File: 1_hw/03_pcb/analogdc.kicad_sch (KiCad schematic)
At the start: 12 parts, among them U25 LM6171, U26 TMUX6104

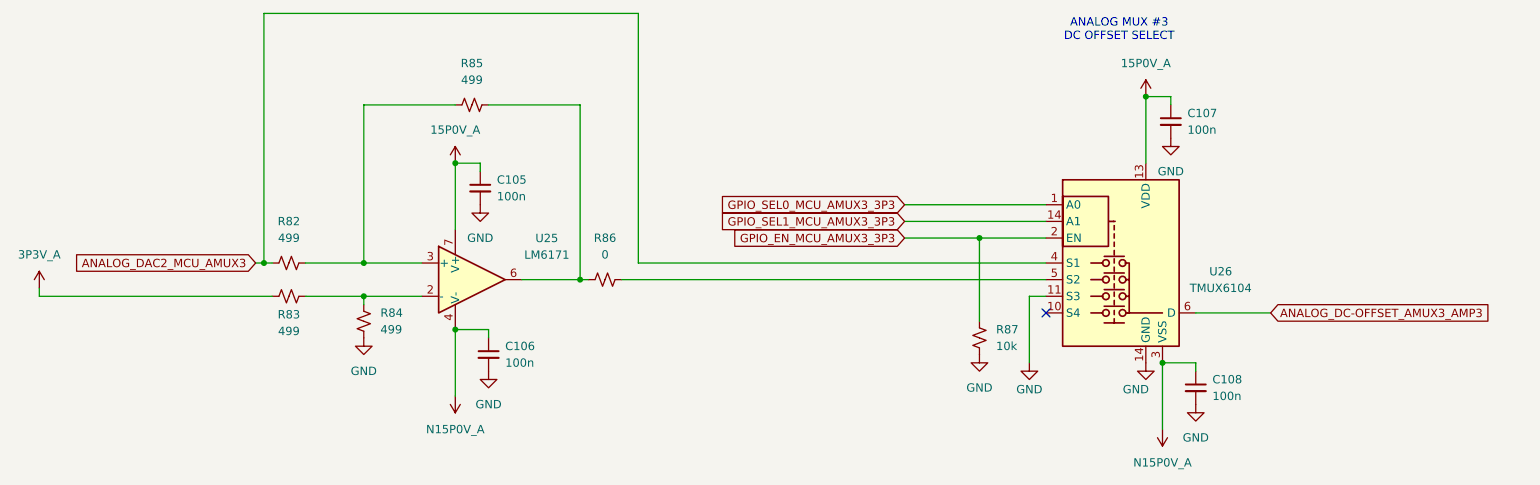
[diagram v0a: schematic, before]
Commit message: FEAT: Initial board placement started.
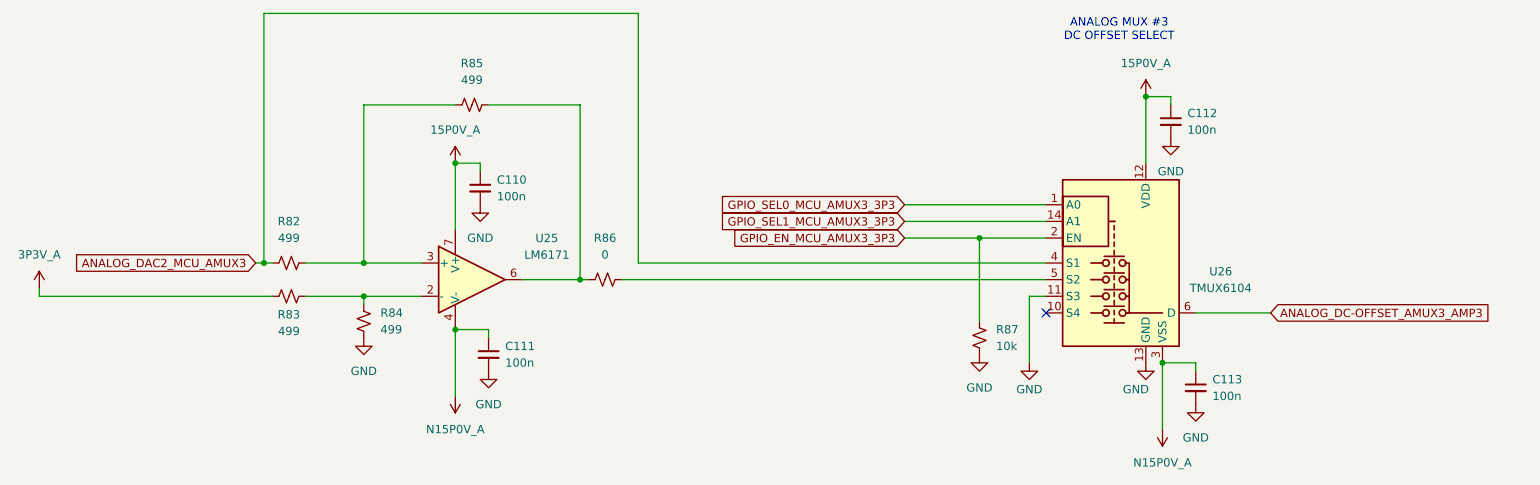
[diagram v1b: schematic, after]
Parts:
- renumbered C105 to C110, C106 to C111, C107 to C112, C108 to C113
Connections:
- net 15P0V_A: now also U26.12 (VDD); no longer U26.13 (VDD)
- net GND: now also U26.13 (GND); no longer U26.14 (A1)
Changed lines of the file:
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@@
 		(dnp no)
 		(fields_autoplaced yes)
-		(property "Reference" "C106"
+		(property "Reference" "C111"
 			(at 111.76 113.0363 0)
 			(effects
@@
 			(project "arb"
 				(path "/866ef9be-3b01-4288-a6e0-a2357aa17e50/dd20ed2c-105a-40ef-bdba-a4198899f68e"
-					(reference "C106")
+					(reference "C111")
 					(unit 1)
 				)
@@
 		(on_board yes)
 		(dnp no)
-		(property "Reference" "#PWR0277"
+		(property "Reference" "#PWR0289"
 			(at 209.55 121.92 0)
 			(effects
@@
 			(project "arb"
 				(path "/866ef9be-3b01-4288-a6e0-a2357aa17e50/dd20ed2c-105a-40ef-bdba-a4198899f68e"
-					(reference "#PWR0277")
+					(reference "#PWR0289")
 					(unit 1)
 				)
@@
 		(on_board yes)
 		(dnp no)
-		(property "Reference" "#PWR0275"
+		(property "Reference" "#PWR0287"
 			(at 191.77 121.92 0)
 			(effects
@@
 			(project "arb"
 				(path "/866ef9be-3b01-4288-a6e0-a2357aa17e50/dd20ed2c-105a-40ef-bdba-a4198899f68e"
-					(reference "#PWR0275")
+					(reference "#PWR0287")
 					(unit 1)
 				)
@@
 		(dnp no)
 		(fields_autoplaced yes)
-		(property "Reference" "#PWR0268"
+		(property "Reference" "#PWR0280"
 			(at 40.64 107.95 0)
 			(effects
@@
 			(project "arb"
 				(path "/866ef9be-3b01-4288-a6e0-a2357aa17e50/dd20ed2c-105a-40ef-bdba-a4198899f68e"
-					(reference "#PWR0268")
+					(reference "#PWR0280")
 					(unit 1)
 				)
@@
 		(dnp no)
 		(fields_autoplaced yes)
-		(property "Reference" "#PWR0279"
+		(property "Reference" "#PWR0291"
 			(at 213.36 87.63 0)
 			(effects
@@
 			(project "arb"
 				(path "/866ef9be-3b01-4288-a6e0-a2357aa17e50/dd20ed2c-105a-40ef-bdba-a4198899f68e"
-					(reference "#PWR0279")
+					(reference "#PWR0291")
 					(unit 1)
 				)
@@
 		(dnp no)
 		(fields_autoplaced yes)
-		(property "Reference" "#PWR0269"
+		(property "Reference" "#PWR0281"
 			(at 90.17 118.11 0)
 			(effects
@@
 			(project "arb"
 				(path "/866ef9be-3b01-4288-a6e0-a2357aa17e50/dd20ed2c-105a-40ef-bdba-a4198899f68e"
-					(reference "#PWR0269")
+					(reference "#PWR0281")
 					(unit 1)
 				)
@@
 		(dnp no)
 		(fields_autoplaced yes)
-		(property "Reference" "#PWR0273"
+		(property "Reference" "#PWR0285"
 			(at 109.22 123.19 0)
 			(effects
@@
 			(project "arb"
 				(path "/866ef9be-3b01-4288-a6e0-a2357aa17e50/dd20ed2c-105a-40ef-bdba-a4198899f68e"
-					(reference "#PWR0273")
+					(reference "#PWR0285")
 					(unit 1)
 				)
@@
 		(dnp no)
 		(fields_autoplaced yes)
-		(property "Reference" "#PWR0271"
+		(property "Reference" "#PWR0283"
 			(at 104.14 116.84 0)
 			(effects
@@
 			(project "arb"
 				(path "/866ef9be-3b01-4288-a6e0-a2357aa17e50/dd20ed2c-105a-40ef-bdba-a4198899f68e"
-					(reference "#PWR0271")
+					(reference "#PWR0283")
 					(unit 1)
 				)
@@
 		(dnp no)
 		(fields_autoplaced yes)
-		(property "Reference" "#PWR0270"
+		(property "Reference" "#PWR0282"
 			(at 104.14 88.9 0)
 			(effects
@@
 			(project "arb"
 				(path "/866ef9be-3b01-4288-a6e0-a2357aa17e50/dd20ed2c-105a-40ef-bdba-a4198899f68e"
-					(reference "#PWR0270")
+					(reference "#PWR0282")
 					(unit 1)
 				)
@@
 		(dnp no)
 		(fields_autoplaced yes)
-		(property "Reference" "#PWR0274"
+		(property "Reference" "#PWR0286"
 			(at 184.15 120.65 0)
 			(effects
@@
 			(project "arb"
 				(path "/866ef9be-3b01-4288-a6e0-a2357aa17e50/dd20ed2c-105a-40ef-bdba-a4198899f68e"
-					(reference "#PWR0274")
+					(reference "#PWR0286")
 					(unit 1)
 				)
@@
 		(dnp no)
 		(fields_autoplaced yes)
-		(property "Reference" "C108"
+		(property "Reference" "C113"
 			(at 219.71 118.1163 0)
 			(effects
@@
 			(project "arb"
 				(path "/866ef9be-3b01-4288-a6e0-a2357aa17e50/dd20ed2c-105a-40ef-bdba-a4198899f68e"
-					(reference "C108")
+					(reference "C113")
 					(unit 1)
 				)
@@
 		(dnp no)
 		(fields_autoplaced yes)
-		(property "Reference" "#PWR0276"
+		(property "Reference" "#PWR0288"
 			(at 209.55 78.74 0)
 			(effects
@@
 			(project "arb"
 				(path "/866ef9be-3b01-4288-a6e0-a2357aa17e50/dd20ed2c-105a-40ef-bdba-a4198899f68e"
-					(reference "#PWR0276")
+					(reference "#PWR0288")
 					(unit 1)
 				)
@@
 		(dnp no)
 		(fields_autoplaced yes)
-		(property "Reference" "C107"
+		(property "Reference" "C112"
 			(at 215.9 77.4763 0)
 			(effects
@@
 			(project "arb"
 				(path "/866ef9be-3b01-4288-a6e0-a2357aa17e50/dd20ed2c-105a-40ef-bdba-a4198899f68e"
-					(reference "C107")
+					(reference "C112")
 					(unit 1)
 				)
@@
 		(dnp no)
 		(fields_autoplaced yes)
-		(property "Reference" "#PWR0278"
+		(property "Reference" "#PWR0290"
 			(at 212.09 121.92 0)
 			(effects
@@
 			(project "arb"
 				(path "/866ef9be-3b01-4288-a6e0-a2357aa17e50/dd20ed2c-105a-40ef-bdba-a4198899f68e"
-					(reference "#PWR0278")
+					(reference "#PWR0290")
 					(unit 1)
 				)
@@
 		(pin "7"
 		)
-		(pin "14"
+		(pin "12"
 		)
 		(pin "1"
@@
 		(dnp no)
 		(fields_autoplaced yes)
-		(property "Reference" "#PWR0280"
+		(property "Reference" "#PWR0292"
 			(at 217.17 128.27 0)
 			(effects
@@
 			(project "arb"
 				(path "/866ef9be-3b01-4288-a6e0-a2357aa17e50/dd20ed2c-105a-40ef-bdba-a4198899f68e"
-					(reference "#PWR0280")
+					(reference "#PWR0292")
 					(unit 1)
 				)
@@
 		(dnp no)
 		(fields_autoplaced yes)
-		(property "Reference" "#PWR0272"
+		(property "Reference" "#PWR0284"
 			(at 107.95 97.79 0)
 			(effects
@@
 			(project "arb"
 				(path "/866ef9be-3b01-4288-a6e0-a2357aa17e50/dd20ed2c-105a-40ef-bdba-a4198899f68e"
-					(reference "#PWR0272")
+					(reference "#PWR0284")
 					(unit 1)
 				)
@@
 		(dnp no)
 		(fields_autoplaced yes)
-		(property "Reference" "C105"
+		(property "Reference" "C110"
 			(at 110.49 87.6363 0)
 			(effects
@@
 			(project "arb"
 				(path "/866ef9be-3b01-4288-a6e0-a2357aa17e50/dd20ed2c-105a-40ef-bdba-a4198899f68e"
-					(reference "C105")
-					(unit 1)
-				)
+					(reference "C110")
+					(unit 1)
+				)

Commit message: FEAT: Changed Inductor to higher current. Continued layout. Assigned some Netclasses.
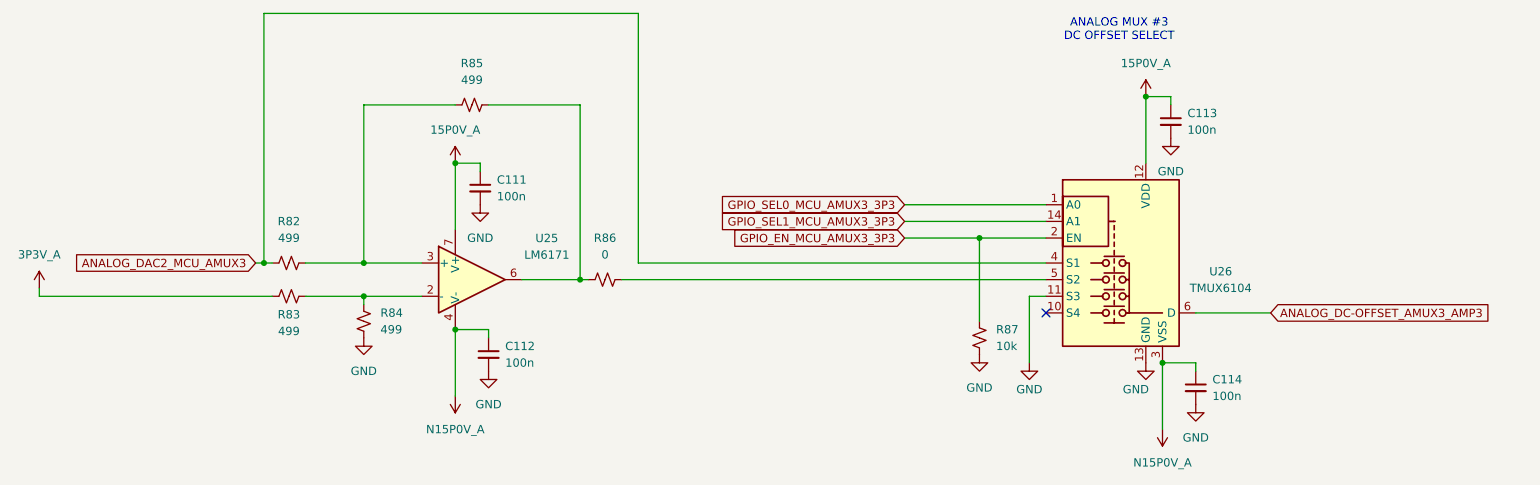
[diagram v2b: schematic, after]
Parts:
- renumbered C110 to C111, C111 to C112, C112 to C113, C113 to C114
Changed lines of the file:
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@@
 		(dnp no)
 		(fields_autoplaced yes)
-		(property "Reference" "C111"
+		(property "Reference" "C112"
 			(at 111.76 113.0363 0)
 			(effects
@@
 			(project "arb"
 				(path "/866ef9be-3b01-4288-a6e0-a2357aa17e50/dd20ed2c-105a-40ef-bdba-a4198899f68e"
-					(reference "C111")
+					(reference "C112")
 					(unit 1)
 				)
@@
 		(on_board yes)
 		(dnp no)
-		(property "Reference" "#PWR0289"
+		(property "Reference" "#PWR0291"
 			(at 209.55 121.92 0)
 			(effects
@@
 			(project "arb"
 				(path "/866ef9be-3b01-4288-a6e0-a2357aa17e50/dd20ed2c-105a-40ef-bdba-a4198899f68e"
-					(reference "#PWR0289")
+					(reference "#PWR0291")
 					(unit 1)
 				)
@@
 		(on_board yes)
 		(dnp no)
-		(property "Reference" "#PWR0287"
+		(property "Reference" "#PWR0289"
 			(at 191.77 121.92 0)
 			(effects
@@
 			(project "arb"
 				(path "/866ef9be-3b01-4288-a6e0-a2357aa17e50/dd20ed2c-105a-40ef-bdba-a4198899f68e"
-					(reference "#PWR0287")
+					(reference "#PWR0289")
 					(unit 1)
 				)
@@
 		(dnp no)
 		(fields_autoplaced yes)
-		(property "Reference" "#PWR0280"
+		(property "Reference" "#PWR0282"
 			(at 40.64 107.95 0)
 			(effects
@@
 			(project "arb"
 				(path "/866ef9be-3b01-4288-a6e0-a2357aa17e50/dd20ed2c-105a-40ef-bdba-a4198899f68e"
-					(reference "#PWR0280")
+					(reference "#PWR0282")
 					(unit 1)
 				)
@@
 		(dnp no)
 		(fields_autoplaced yes)
-		(property "Reference" "#PWR0291"
+		(property "Reference" "#PWR0293"
 			(at 213.36 87.63 0)
 			(effects
@@
 			(project "arb"
 				(path "/866ef9be-3b01-4288-a6e0-a2357aa17e50/dd20ed2c-105a-40ef-bdba-a4198899f68e"
-					(reference "#PWR0291")
+					(reference "#PWR0293")
 					(unit 1)
 				)
@@
 		(dnp no)
 		(fields_autoplaced yes)
-		(property "Reference" "#PWR0281"
+		(property "Reference" "#PWR0283"
 			(at 90.17 118.11 0)
 			(effects
@@
 			(project "arb"
 				(path "/866ef9be-3b01-4288-a6e0-a2357aa17e50/dd20ed2c-105a-40ef-bdba-a4198899f68e"
-					(reference "#PWR0281")
+					(reference "#PWR0283")
 					(unit 1)
 				)
@@
 		(dnp no)
 		(fields_autoplaced yes)
-		(property "Reference" "#PWR0285"
+		(property "Reference" "#PWR0287"
 			(at 109.22 123.19 0)
 			(effects
@@
 			(project "arb"
 				(path "/866ef9be-3b01-4288-a6e0-a2357aa17e50/dd20ed2c-105a-40ef-bdba-a4198899f68e"
-					(reference "#PWR0285")
+					(reference "#PWR0287")
 					(unit 1)
 				)
@@
 		(dnp no)
 		(fields_autoplaced yes)
-		(property "Reference" "#PWR0283"
+		(property "Reference" "#PWR0285"
 			(at 104.14 116.84 0)
 			(effects
@@
 			(project "arb"
 				(path "/866ef9be-3b01-4288-a6e0-a2357aa17e50/dd20ed2c-105a-40ef-bdba-a4198899f68e"
-					(reference "#PWR0283")
+					(reference "#PWR0285")
 					(unit 1)
 				)
@@
 		(dnp no)
 		(fields_autoplaced yes)
-		(property "Reference" "#PWR0282"
+		(property "Reference" "#PWR0284"
 			(at 104.14 88.9 0)
 			(effects
@@
 			(project "arb"
 				(path "/866ef9be-3b01-4288-a6e0-a2357aa17e50/dd20ed2c-105a-40ef-bdba-a4198899f68e"
-					(reference "#PWR0282")
+					(reference "#PWR0284")
 					(unit 1)
 				)
@@
 		(dnp no)
 		(fields_autoplaced yes)
-		(property "Reference" "#PWR0286"
+		(property "Reference" "#PWR0288"
 			(at 184.15 120.65 0)
 			(effects
@@
 			(project "arb"
 				(path "/866ef9be-3b01-4288-a6e0-a2357aa17e50/dd20ed2c-105a-40ef-bdba-a4198899f68e"
-					(reference "#PWR0286")
+					(reference "#PWR0288")
 					(unit 1)
 				)
@@
 		(dnp no)
 		(fields_autoplaced yes)
-		(property "Reference" "C113"
+		(property "Reference" "C114"
 			(at 219.71 118.1163 0)
 			(effects
@@
 			(project "arb"
 				(path "/866ef9be-3b01-4288-a6e0-a2357aa17e50/dd20ed2c-105a-40ef-bdba-a4198899f68e"
-					(reference "C113")
+					(reference "C114")
 					(unit 1)
 				)
@@
 		(dnp no)
 		(fields_autoplaced yes)
-		(property "Reference" "#PWR0288"
+		(property "Reference" "#PWR0290"
 			(at 209.55 78.74 0)
 			(effects
@@
 			(project "arb"
 				(path "/866ef9be-3b01-4288-a6e0-a2357aa17e50/dd20ed2c-105a-40ef-bdba-a4198899f68e"
-					(reference "#PWR0288")
+					(reference "#PWR0290")
 					(unit 1)
 				)
@@
 		(dnp no)
 		(fields_autoplaced yes)
-		(property "Reference" "C112"
+		(property "Reference" "C113"
 			(at 215.9 77.4763 0)
 			(effects
@@
 			(project "arb"
 				(path "/866ef9be-3b01-4288-a6e0-a2357aa17e50/dd20ed2c-105a-40ef-bdba-a4198899f68e"
-					(reference "C112")
+					(reference "C113")
 					(unit 1)
 				)
@@
 		(dnp no)
 		(fields_autoplaced yes)
-		(property "Reference" "#PWR0290"
+		(property "Reference" "#PWR0292"
 			(at 212.09 121.92 0)
 			(effects
@@
 			(project "arb"
 				(path "/866ef9be-3b01-4288-a6e0-a2357aa17e50/dd20ed2c-105a-40ef-bdba-a4198899f68e"
-					(reference "#PWR0290")
+					(reference "#PWR0292")
 					(unit 1)
 				)
@@
 		(dnp no)
 		(fields_autoplaced yes)
-		(property "Reference" "#PWR0292"
+		(property "Reference" "#PWR0294"
 			(at 217.17 128.27 0)
 			(effects
@@
 			(project "arb"
 				(path "/866ef9be-3b01-4288-a6e0-a2357aa17e50/dd20ed2c-105a-40ef-bdba-a4198899f68e"
-					(reference "#PWR0292")
+					(reference "#PWR0294")
 					(unit 1)
 				)
@@
 		(dnp no)
 		(fields_autoplaced yes)
-		(property "Reference" "#PWR0284"
+		(property "Reference" "#PWR0286"
 			(at 107.95 97.79 0)
 			(effects
@@
 			(project "arb"
 				(path "/866ef9be-3b01-4288-a6e0-a2357aa17e50/dd20ed2c-105a-40ef-bdba-a4198899f68e"
-					(reference "#PWR0284")
+					(reference "#PWR0286")
 					(unit 1)
 				)
@@
 		(dnp no)
 		(fields_autoplaced yes)
-		(property "Reference" "C110"
+		(property "Reference" "C111"
 			(at 110.49 87.6363 0)
 			(effects
@@
 			(project "arb"
 				(path "/866ef9be-3b01-4288-a6e0-a2357aa17e50/dd20ed2c-105a-40ef-bdba-a4198899f68e"
-					(reference "C110")
-					(unit 1)
-				)
+					(reference "C111")
+					(unit 1)
+				)

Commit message: FEAT: Finished DDS, MCU Layout.
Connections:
- net ANALOG_DAC2_MCU_AMUX3: now also R82.2; no longer R82.1
- net at R85.1, U25.3 (+): now also R82.1; no longer R82.2
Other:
- moved on the sheet: R82
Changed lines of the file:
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@@
 	(symbol
 		(lib_id "Device:R_Small_US")
-		(at 78.74 100.33 90)
+		(at 78.74 100.33 270)
+		(mirror x)
 		(unit 1)
 		(exclude_from_sim no)
@@
 		(on_board yes)
 		(dnp no)
-		(fields_autoplaced yes)
 		(property "Reference" "R82"
 			(at 78.74 93.98 90)
